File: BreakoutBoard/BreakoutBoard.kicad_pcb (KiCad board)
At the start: 2 copper layers, 43.2 x 53.3 mm, 30 parts, among them J1 addon_conn, J2 Power_top, J3 Power_bottom, J4 Conn_01x09, J5 Conn_01x10

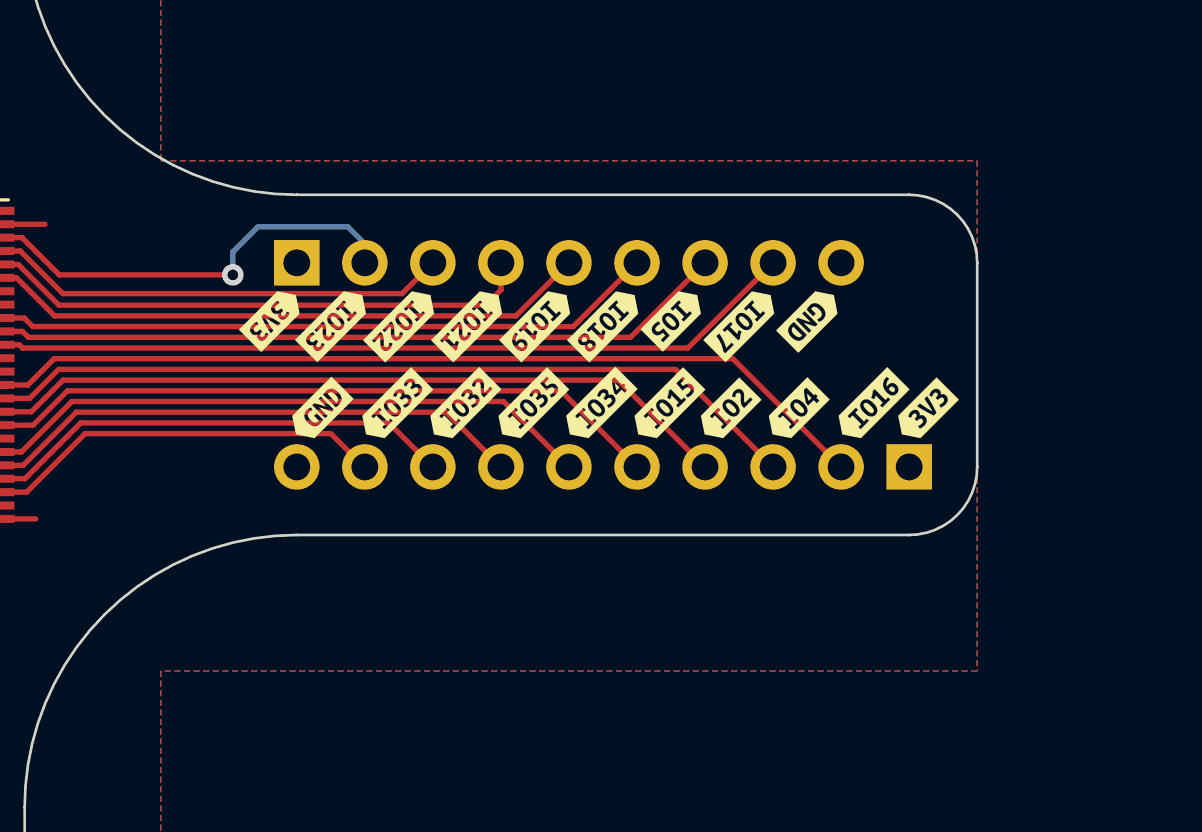
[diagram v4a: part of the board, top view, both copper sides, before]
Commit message: Adds temporary logo to the breakout board
This increases the width of the board a bit, but that should matter
much, specially since it's still smaller than the base board.
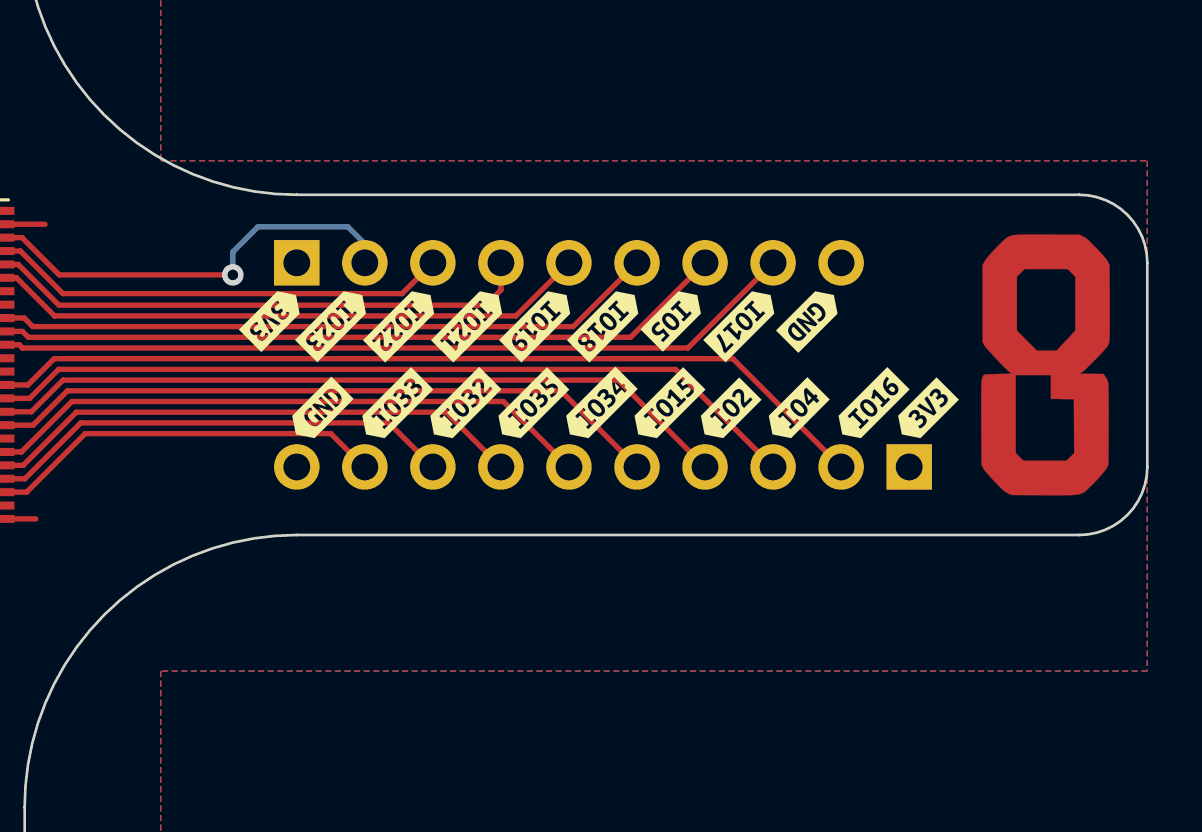
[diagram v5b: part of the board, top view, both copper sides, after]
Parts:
- added Ref**: Val**, GameOver:logo_fcu, F.Cu at (172.7, 99.1)
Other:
- board size 43.2 x 53.3 mm -> 49.5 x 53.3 mm

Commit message: Adds revision number to PCBs
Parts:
- added kibuzzard-62599743: G***, kibuzzard-62599743, B.Cu at (156.2, 99.1)

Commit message: Adds JLCPCB order number placeholder to breakout board
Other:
- board text added: "JLCJLCJLCJLC"
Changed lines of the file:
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@@
       (outputformat 1)
       (mirror false)
-      (drillshape 1)
+      (drillshape 0)
       (scaleselection 1)
-      (outputdirectory "")
+      (outputdirectory "Gerber/")
     )
   )
@@
   (gr_arc (start 176.53 102.87) (mid 175.786051 104.666051) (end 173.99 105.41)
     (stroke (width 0.1) (type default)) (layer "Edge.Cuts"))
+  (gr_text "JLCJLCJLCJLC" (at 131 99 90) (layer "F.SilkS")
+    (effects (font (size 1 1) (thickness 0.25) bold))
+  )
   (gr_text "Power_top" (at 130.81 124.993949 180) (layer "B.Fab")
     (effects (font (size 1 1) (thickness 0.15)) (justify mirror))
